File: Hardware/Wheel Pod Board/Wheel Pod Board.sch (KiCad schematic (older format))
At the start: 31 parts, among them J1 Conn_RJ-45, P1 UIM240XX_Stepper_Conn, P2 RS232, P3 ST_SWD_Connector, P4 RS485, P5 BATT, P6 SyRen Pwr, U1 STM32F401RCT6, U2 SN75176BDR, U3 ZXCT1107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

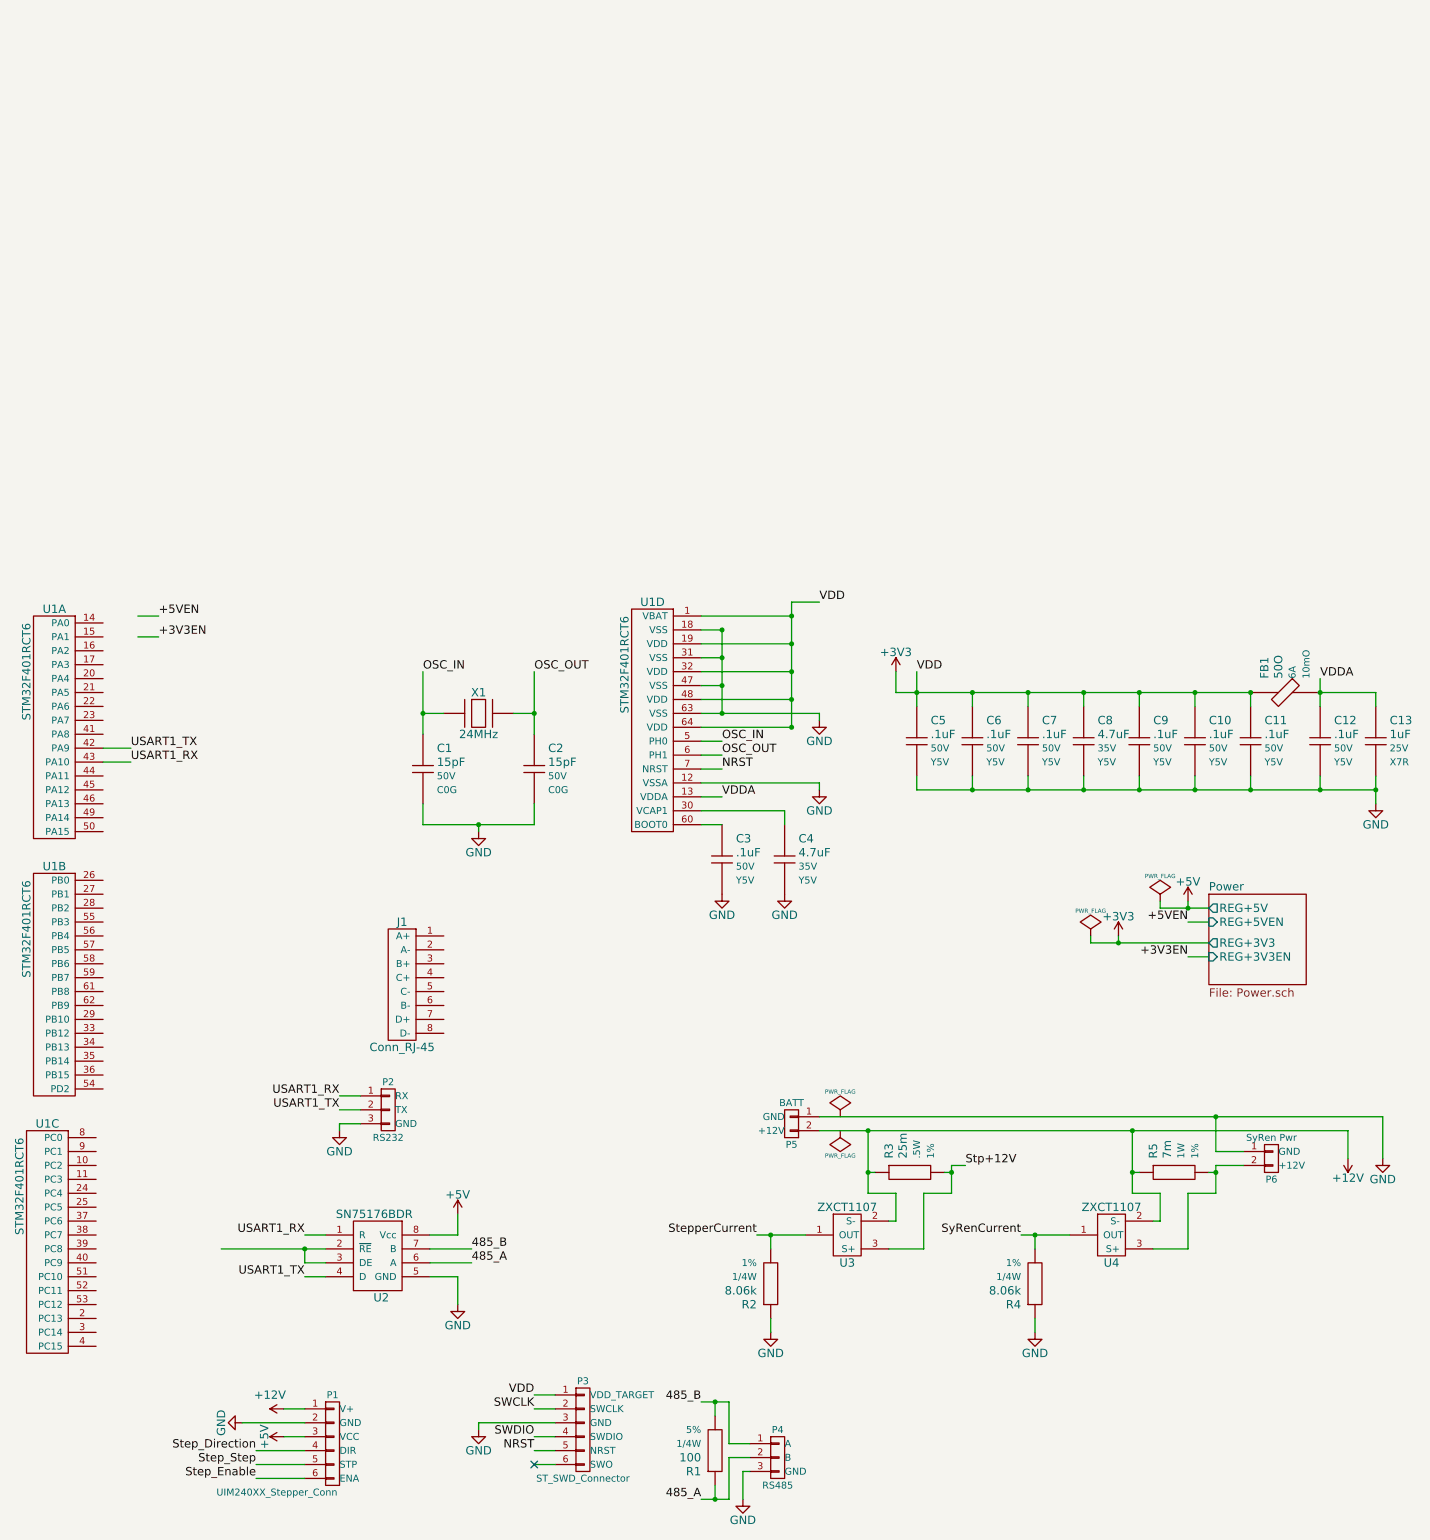
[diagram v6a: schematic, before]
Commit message: Connect 485 to RJ45 jack on schematic
#5
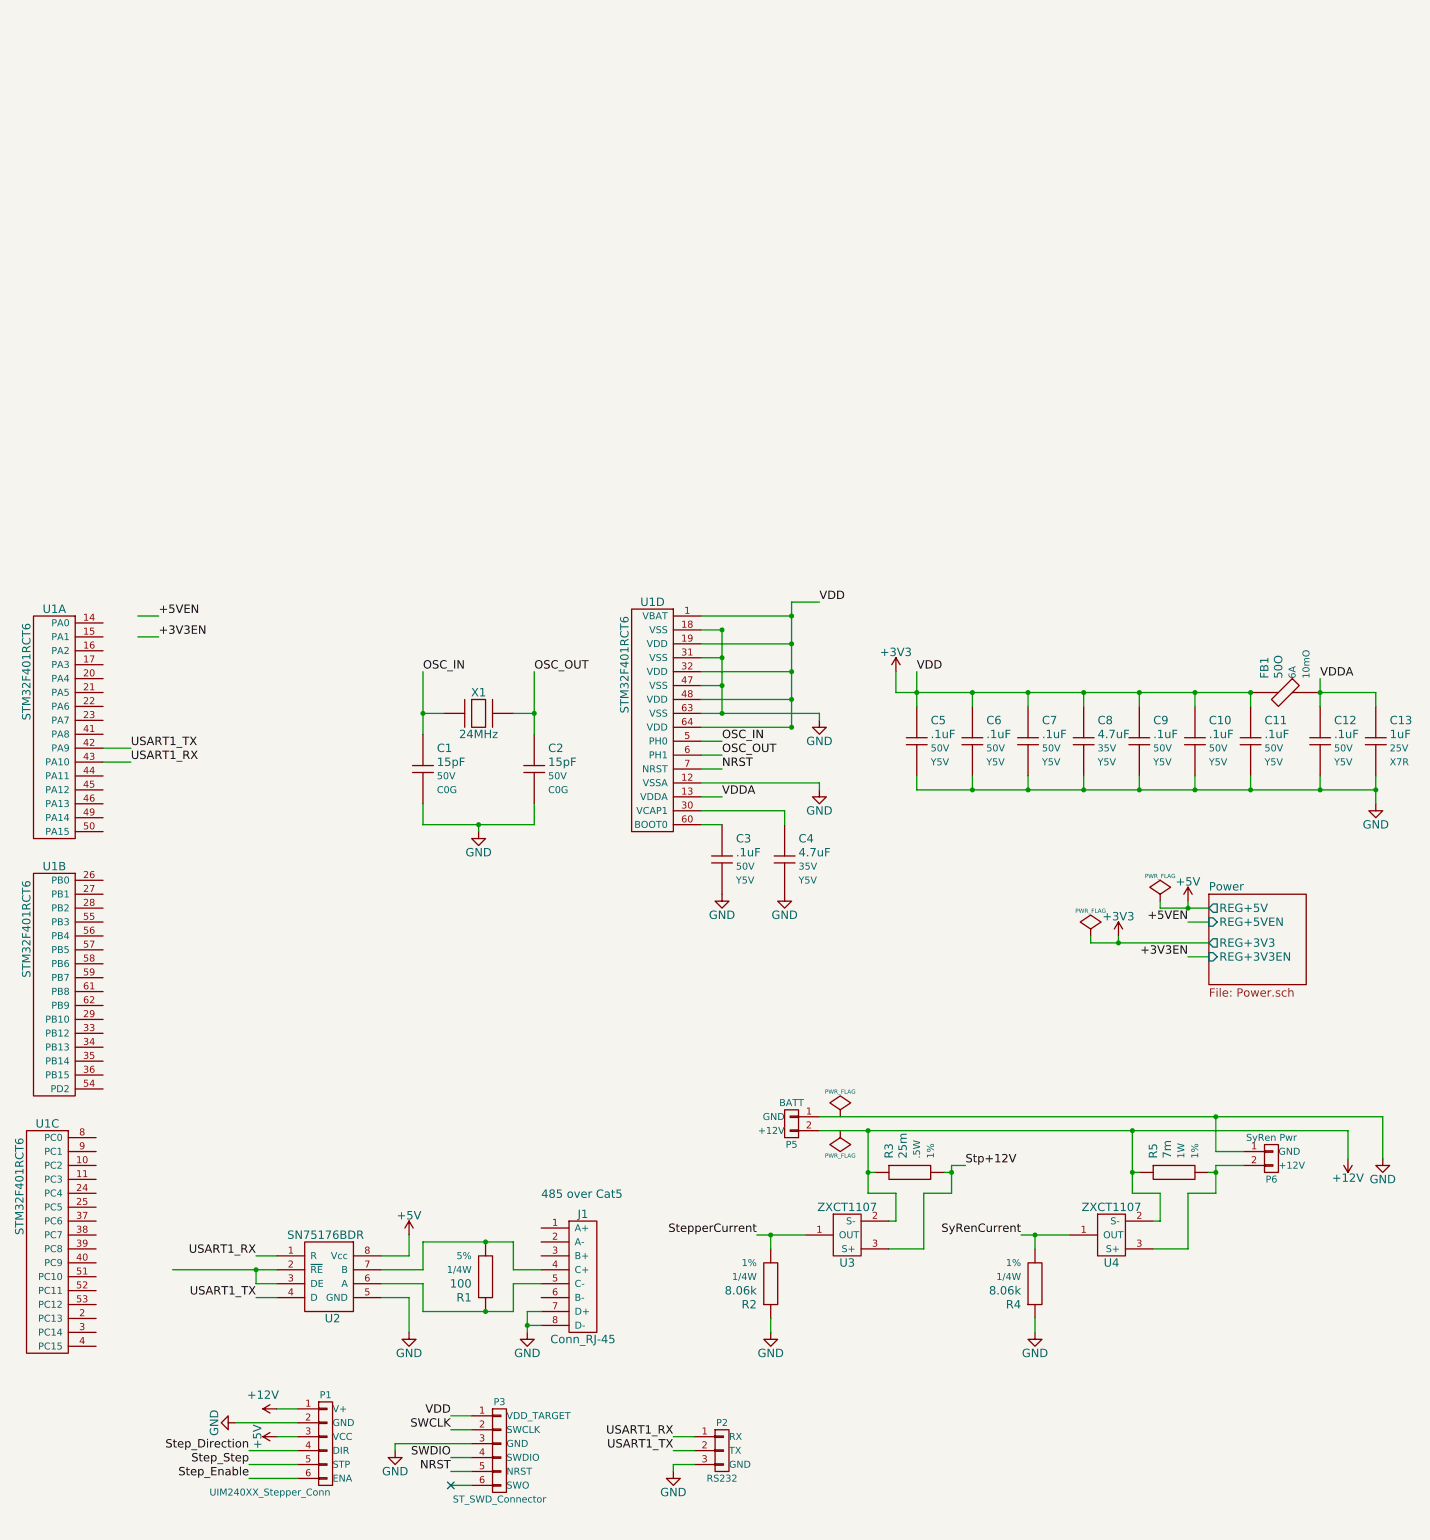
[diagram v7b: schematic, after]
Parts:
- removed P4: RS485, MAVRIC_footprints:1x3_SMD_header, symbol RS485
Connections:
- net 485_A is gone; now on an unnamed net: R1.1, U2.6 (A)
- net 485_B is gone; now on an unnamed net: R1.2, U2.7 (B)
- net GND: now also J1.7 (D+), J1.8 (D-)
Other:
- note added: "485 over Cat5"
- moved on the sheet: J1, P1, P2, P3, R1, U2

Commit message: Fix footprints, add RJ45 jack to pcb
Resolve #12, Resolve #5
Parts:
- U2: footprint SMD_Packages:SOIC-8-W -> Housings_SOIC:SOIC-8_3.9x4.9mm_Pitch1.27mm
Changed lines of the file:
@@
 F 0 "U2" H 3300 5250 60  0000 C CNN
 F 1 "SN75176BDR" H 3250 5850 60  0000 C CNN
-F 2 "SMD_Packages:SOIC-8-W" H 3450 5700 60  0001 C CNN
+F 2 "Housings_SOIC:SOIC-8_3.9x4.9mm_Pitch1.27mm" H 3450 5700 60  0001 C CNN
 F 3 "" H 3450 5700 60  0000 C CNN
 	1    3450 5700
